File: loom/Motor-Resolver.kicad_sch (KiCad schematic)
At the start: 3 parts, among them J20 Resolver, J21 Temperature Sensor, J25 Motor Casing

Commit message: fix(Loom): changed names of netlists
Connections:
- net Motor.Casing.GND renamed MOTOR.CASING.GND
- net Resolver.Cos+ renamed RESOLVER.COS+
- net Resolver.Cos- renamed RESOLVER.COS-
- net Resolver.EXC renamed RESOLVER.EXC
- net Resolver.GND renamed RESOLVER.GND
- net Resolver.Shield.GND renamed RESOLVER.SHIELD.GND
- net Resolver.Sin+ renamed RESOLVER.SIN+
- net Resolver.Sin- renamed RESOLVER.SIN-
- net Temp.Sensor.EXC renamed TEMP.SENSOR.EXC
- net Temp.Sensor.GND renamed TEMP.SENSOR.GND
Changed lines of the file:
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@@
 (kicad_sch (version 20230121) (generator eeschema)
   (paper "A4")
-  (bus_alias "Motor.Inverter" (members "Resolver.EXC" "Resolver.Sin+" "Resolver.Sin-" "Resolver.Cos+" "Resolver.Cos-" "Resolver.GND" "Resolver.Shield.GND" "Temp.Sensor.EXC" "Temp.Sensor.GND" "Motor.Casing.GND"))
+  (bus_alias "Motor.Inverter" (members "RESOLVER.EXC" "RESOLVER.Sin+" "RESOLVER.Sin-" "RESOLVER.Cos+" "RESOLVER.Cos-" "RESOLVER.GND" "RESOLVER.SHIELD.GND" "TEMP.SENSOR.EXC" "TEMP.SENSOR.GND" "MOTOR.CASING.GND"))
   (junction (at 161.29 45.72) (diameter 0) (color 0 0 0 0)
   )
@@
     (stroke (width 0) (type default))
   )
-  (label "Resolver.EXC" (at 137.16 57.15 0) (fields_autoplaced)
+  (label "RESOLVER.EXC" (at 137.16 57.15 0) (fields_autoplaced)
     (effects (font (size 1.27 1.27)) (justify left bottom))
   )
-  (label "Motor.Casing.GND" (at 181.61 38.1 180) (fields_autoplaced)
+  (label "MOTOR.CASING.GND" (at 181.61 38.1 180) (fields_autoplaced)
     (effects (font (size 1.27 1.27)) (justify right bottom))
   )
-  (label "Resolver.Cos+" (at 137.16 64.77 0) (fields_autoplaced)
+  (label "RESOLVER.COS+" (at 137.16 64.77 0) (fields_autoplaced)
     (effects (font (size 1.27 1.27)) (justify left bottom))
   )
-  (label "Resolver.Cos-" (at 137.16 67.31 0) (fields_autoplaced)
+  (label "RESOLVER.COS-" (at 137.16 67.31 0) (fields_autoplaced)
     (effects (font (size 1.27 1.27)) (justify left bottom))
   )
-  (label "Temp.Sensor.EXC" (at 137.16 40.64 0) (fields_autoplaced)
+  (label "TEMP.SENSOR.EXC" (at 137.16 40.64 0) (fields_autoplaced)
     (effects (font (size 1.27 1.27)) (justify left bottom))
   )
-  (label "Resolver.GND" (at 137.16 69.85 0) (fields_autoplaced)
+  (label "RESOLVER.GND" (at 137.16 69.85 0) (fields_autoplaced)
     (effects (font (size 1.27 1.27)) (justify left bottom))
   )
-  (label "Resolver.Sin-" (at 137.16 62.23 0) (fields_autoplaced)
+  (label "RESOLVER.SIN-" (at 137.16 62.23 0) (fields_autoplaced)
     (effects (font (size 1.27 1.27)) (justify left bottom))
   )
-  (label "Resolver.Sin+" (at 137.16 59.69 0) (fields_autoplaced)
+  (label "RESOLVER.SIN+" (at 137.16 59.69 0) (fields_autoplaced)
     (effects (font (size 1.27 1.27)) (justify left bottom))
   )
@@
     (effects (font (size 1.27 1.27)) (justify left bottom))
   )
-  (label "Resolver.Shield.GND" (at 137.16 72.39 0) (fields_autoplaced)
+  (label "RESOLVER.SHIELD.GND" (at 137.16 72.39 0) (fields_autoplaced)
     (effects (font (size 1.27 1.27)) (justify left bottom))
   )
-  (label "Temp.Sensor.GND" (at 137.16 38.1 0) (fields_autoplaced)
+  (label "TEMP.SENSOR.GND" (at 137.16 38.1 0) (fields_autoplaced)
     (effects (font (size 1.27 1.27)) (justify left bottom))
   )

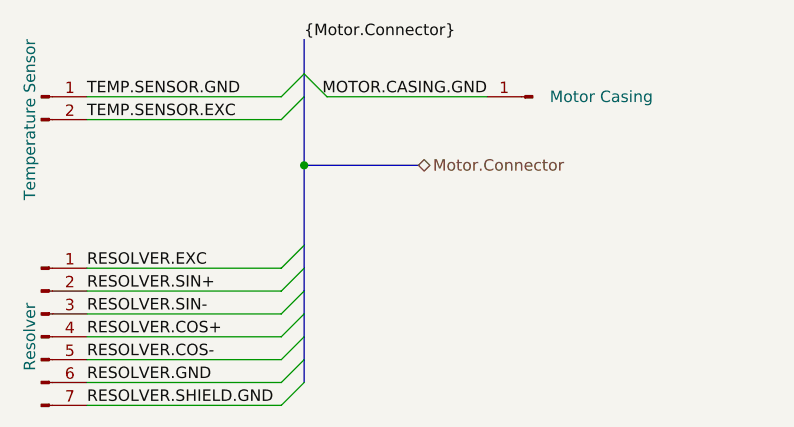
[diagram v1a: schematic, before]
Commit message: feat(Loom): Updated version of Loom Schematic
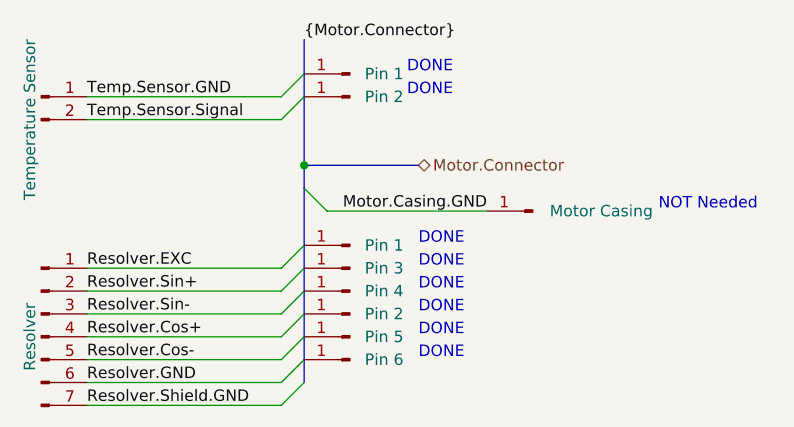
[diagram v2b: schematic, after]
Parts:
- added J173: Pin 6, symbol Connector:Conn_01x01_Pin
- added J174, J88: Pin 1, symbol Connector:Conn_01x01_Pin
- added J175, J196: Pin 2, symbol Connector:Conn_01x01_Pin
- added J176: Pin 5, symbol Connector:Conn_01x01_Pin
- added J177: Pin 3, symbol Connector:Conn_01x01_Pin
- added J178: Pin 4, symbol Connector:Conn_01x01_Pin
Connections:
- net MOTOR.CASING.GND renamed Motor.Casing.GND
- net RESOLVER.COS+ renamed Resolver.Cos+
- net RESOLVER.COS- renamed Resolver.Cos-
- net RESOLVER.EXC renamed Resolver.EXC
- net RESOLVER.GND renamed Resolver.GND
- net RESOLVER.SHIELD.GND renamed Resolver.Shield.GND
- net RESOLVER.SIN+ renamed Resolver.Sin+
- net RESOLVER.SIN- renamed Resolver.Sin-
- net TEMP.SENSOR.EXC renamed Temp.Sensor.Signal
- net TEMP.SENSOR.GND renamed Temp.Sensor.GND
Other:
- note added: "DONE"
- note added: "NOT Needed"
